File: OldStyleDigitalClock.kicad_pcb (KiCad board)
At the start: 2 copper layers, 155 x 85 mm, 89 parts, among them J1 USB_A_OUT, J2 USB_A_OUT, J3 USB_C_IN, SW1 Set minutes, SW2 Set hours, U1 4071, U10 CD4026BE, U11 NE555D, U12 CD4060BE, U13 CD4017BE, U14 CD4017BE, U15 CD4017BE, U2 D168K, U3 CD4026BE, U4 D168K, U5 CD4026BE, U6 4073, U7 D168K, U8 CD4026BE, U9 D168K, Y1 HC49 XTAL (32768 Hz)

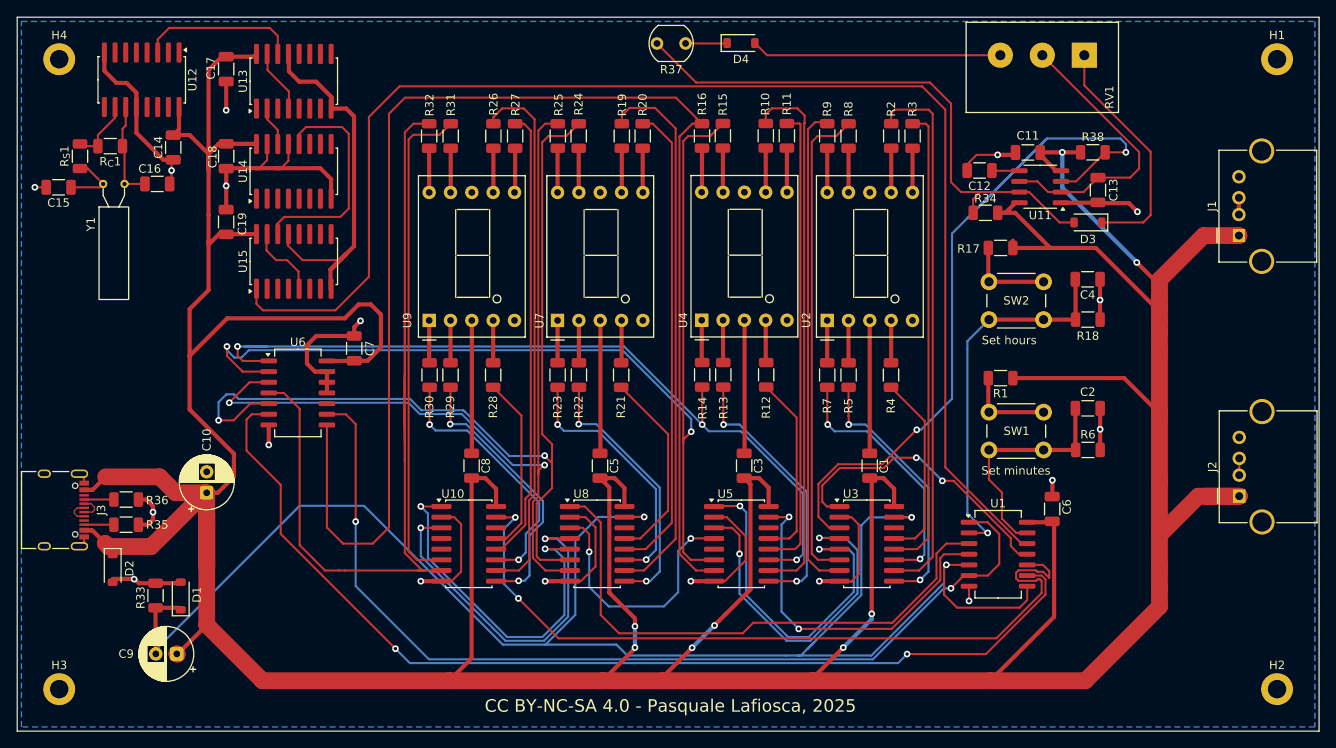
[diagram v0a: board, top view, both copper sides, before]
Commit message: Minor adjustments, moved oscillator away from mounting hole, improved some tracks.
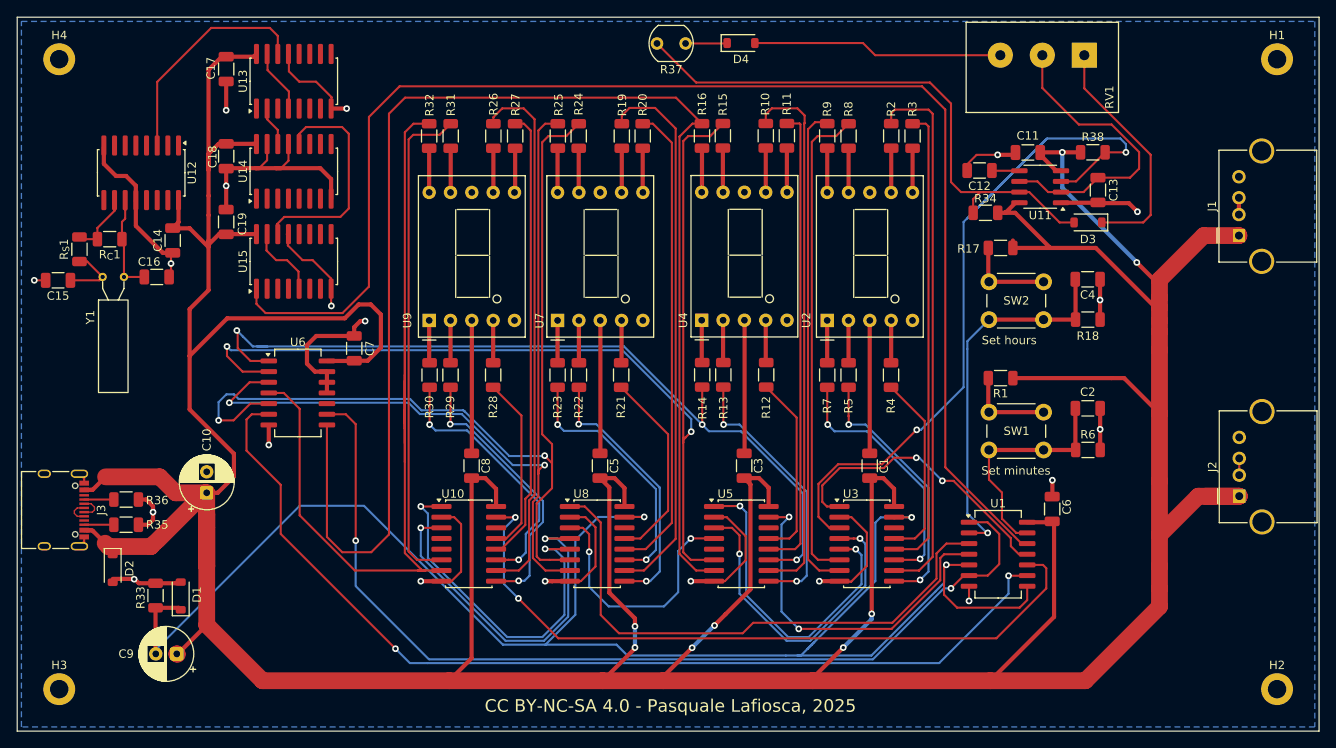
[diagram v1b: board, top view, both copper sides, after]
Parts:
- moved C15 11.1 mm to (54.9, 81.3)
- moved C16 11.1 mm to (66.6, 80.9)
- moved R_{C}1 11.1 mm to (61.0, 76.4)
- moved R_{S}1 11.1 mm to (57.4, 77.6)
- moved Y1 11.1 mm to (60.2, 80.9)
- moved C14 11.1 mm to (68.5, 76.6)
- moved U12 11.1 mm to (64.8, 68.5)
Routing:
- net GND: track 285.6 -> 263.5 mm, vias 18 -> 20
- net /Time/CLK 2 Hz: track 19.0 -> 27.1 mm
- net Net-(U10-RESET): track 93.3 -> 85.4 mm
- net /CLK 1/(24 hours): track 123.2 -> 119.0 mm
- net Net-(U3-CARRY_OUT): track 42.2 -> 38.8 mm
- net Net-(U3-DISPLAY_EN_OUT): track 41.7 -> 38.8 mm
- net Net-(U11-THR): track 34.2 -> 36.5 mm
- net Net-(U10-G): track 128.4 -> 126.3 mm
- net Net-(U5-G): track 167.7 -> 169.7 mm
- net Net-(U5-F): track 128.9 -> 127.9 mm
- net 1_MIN_CLK: track 163.6 -> 164.5 mm
- net MR: track 196.0 -> 195.2 mm

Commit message: Moved USB receptacles, minor changes. Marked no connect pins.
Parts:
- moved J1 3.71 mm to (191.8, 75.9)
- moved J2 3.71 mm to (191.8, 107.0)
- moved J3 0.40 mm to (53.9, 108.7)
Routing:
- net +5V: track 618.9 -> 607.5 mm
- net Net-(J3-D+-PadA6): track 2.93 -> 4.73 mm

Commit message: Reviewed LED limiting resistors to stay within specs
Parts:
- D2: value 1N4733A -> 1N4734A
- R10, R11, R12, R13, R14, R15, R16, R19, R2, R20, R21, R22, R23, R24, R25, R26, R27, R28, R29, R3, R30, R31, R32, R4, R5, R7, R8, R9: value 2.2 kΩ -> 4.7 kΩ

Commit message: Centering
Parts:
- moved C1 0.61 mm to (150.9, 103.4)
- moved C3 0.61 mm to (135.9, 103.4)
- moved R15 0.61 mm to (133.4, 64.1)
- moved R16 0.61 mm to (130.9, 64.1)
- moved R19 0.61 mm to (121.4, 64.1)
- moved R2 0.61 mm to (153.5, 64.1)
- moved R21 0.61 mm to (121.3, 92.6)
- moved R3 0.61 mm to (156.0, 64.1)
- moved R7 0.61 mm to (145.8, 92.6)
- moved R9 0.61 mm to (145.8, 64.1)
- moved U3 0.61 mm to (150.5, 112.7)
- moved C5 0.61 mm to (118.8, 103.4)
- moved C8 0.61 mm to (103.5, 103.4)
- moved R20 0.61 mm to (123.9, 64.1)
- moved R22 0.61 mm to (116.3, 92.6)
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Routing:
- net MR: track 195.2 -> 196.1 mm
- net Net-(U5-G): track 169.7 -> 169.1 mm
- net Net-(U5-E): track 99.2 -> 98.6 mm
- net LED_PWM: track 96.4 -> 97.0 mm
- net Net-(U5-RESET): track 42.5 -> 43.2 mm
- net Net-(U10-RESET): track 85.4 -> 86.0 mm
- net Net-(U8-G): track 106.4 -> 105.8 mm
- net Net-(U8-F): track 112.4 -> 111.8 mm
- net Net-(U8-CLK): track 66.6 -> 67.2 mm
- net Net-(U5-F): track 127.9 -> 127.3 mm
- net Net-(U3-CLK): track 35.3 -> 35.9 mm
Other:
- board text added: ":"

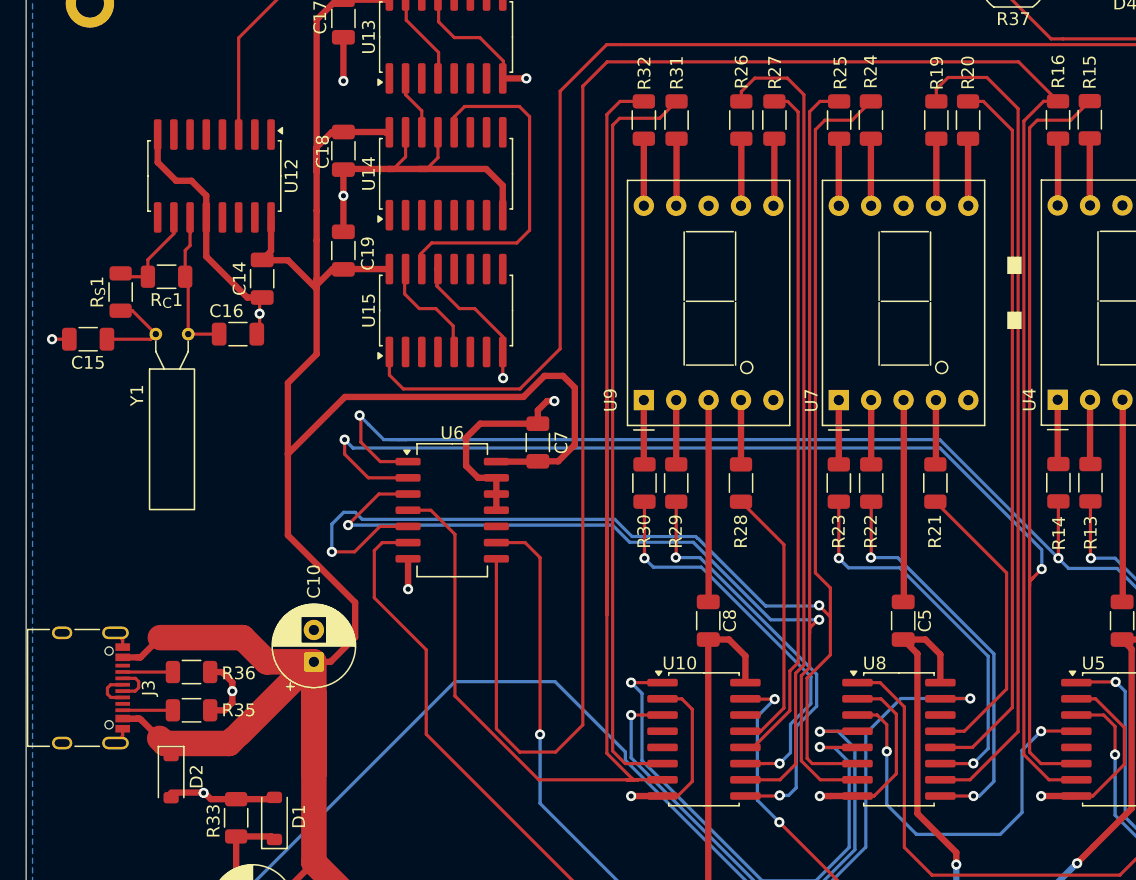
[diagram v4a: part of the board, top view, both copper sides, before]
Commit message: Redesigned USB C input in a more compact way.
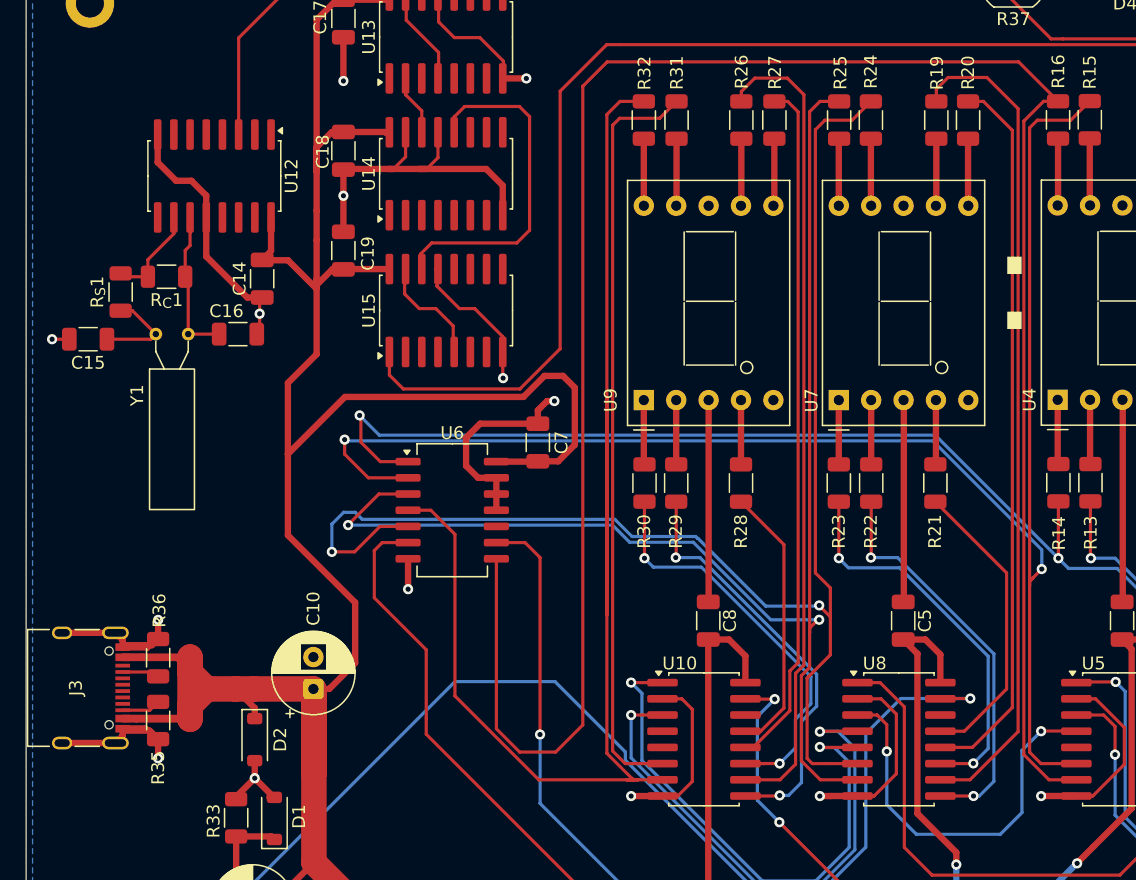
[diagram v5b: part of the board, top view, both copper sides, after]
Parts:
- moved D2 7.17 mm to (67.9, 112.7)
- moved R36 2.85 mm to (60.4, 106.3), turned to 90 degrees
- moved R35 2.74 mm to (60.4, 111.2), turned to -90 degrees
- moved C10 2.13 mm to (72.5, 108.8)
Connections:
- J3 pad A6: Net-(J3-D+-PadA6) -> unconnected-(J3-D+-PadA6)
- J3 pad A7: Net-(J3-D--PadA7) -> unconnected-(J3-D--PadA7)
- J3 pad B6: Net-(J3-D+-PadA6) -> unconnected-(J3-D+-PadB6)
- J3 pad B7: Net-(J3-D--PadA7) -> unconnected-(J3-D--PadB7)
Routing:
- net GND: track 263.5 -> 281.1 mm, vias 20 -> 21
- net +5V: track 607.2 -> 621.9 mm
- net Net-(J3-D+-PadA6): track 4.73 -> 0.00 mm
- net Net-(J3-D--PadA7): track 3.20 -> 0.00 mm
- net Net-(U5-E): track 98.6 -> 97.4 mm
- net Net-(J3-CC1): track 3.54 -> 2.45 mm
- net unconnected-(J3-D+-PadA6): track 0.00 -> 0.83 mm
- net unconnected-(J3-D+-PadB6): track 0.00 -> 0.82 mm

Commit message: Changed footprints for easy to find parts
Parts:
- U1, U6: footprint Package_SO:SO-14_5.3x10.2mm_P1.27mm -> Package_SO:SOIC-14_3.9x8.7mm_P1.27mm
- U10, U12, U13, U14, U15, U3, U5, U8: footprint Package_SO:SOIC-16W_5.3x10.2mm_P1.27mm -> Package_SO:SOP-16_3.9x9.9mm_P1.27mm

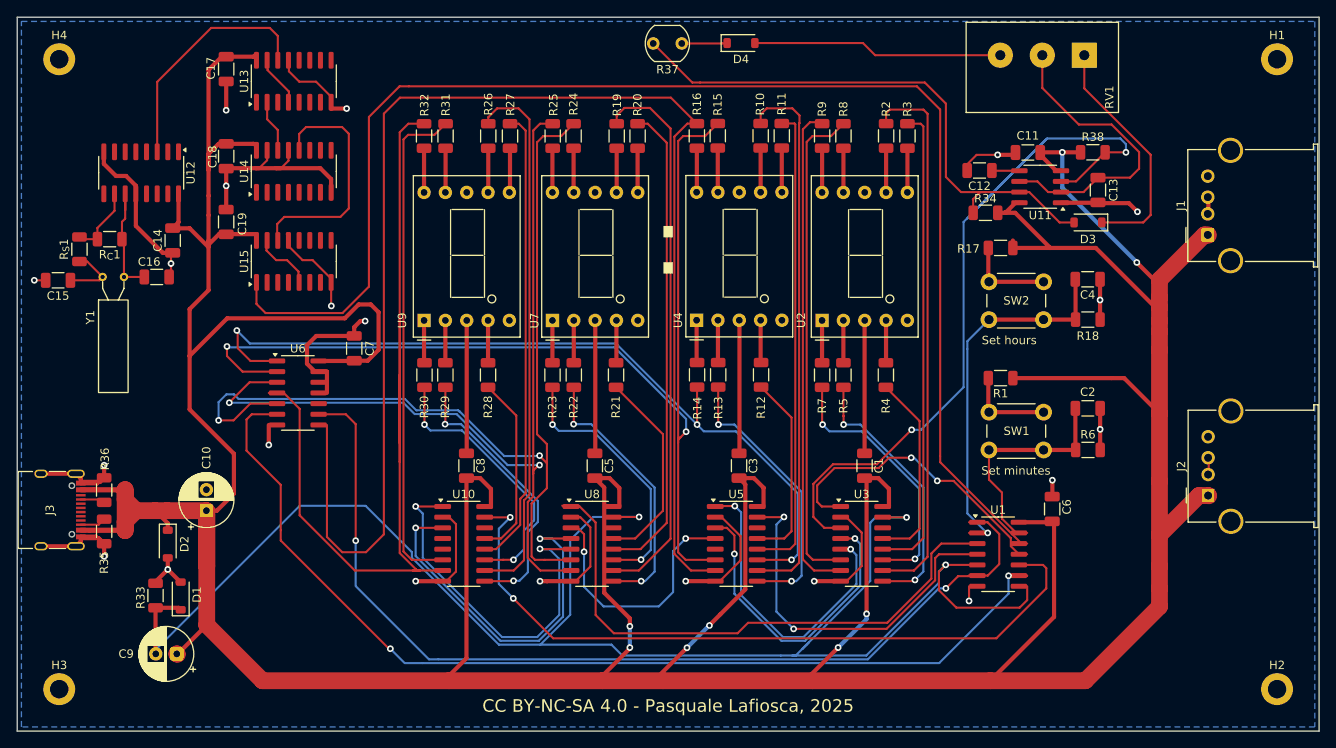
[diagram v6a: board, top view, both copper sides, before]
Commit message: Changed tracks for new IC packages
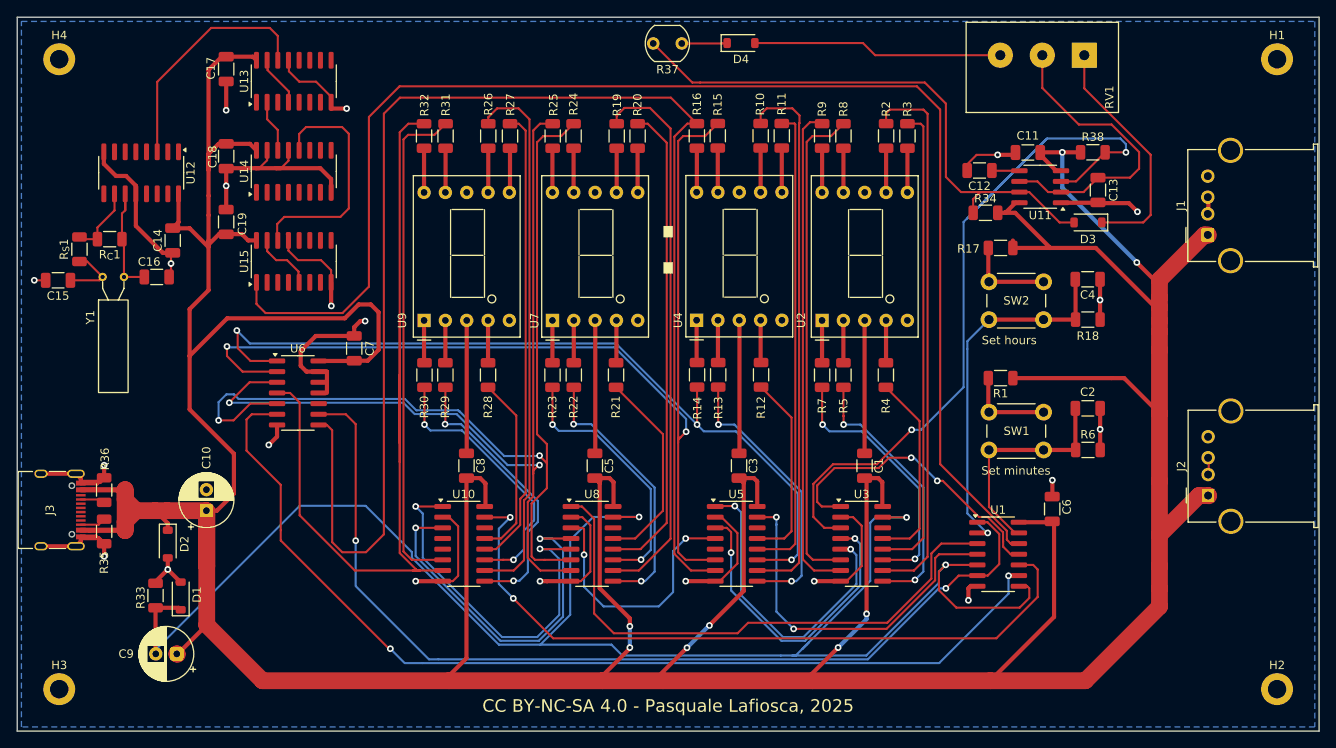
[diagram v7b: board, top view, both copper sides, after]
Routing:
- net GND: track 281.1 -> 288.2 mm
- net Net-(U10-RESET): track 86.0 -> 84.4 mm
- net +5V: track 621.9 -> 623.4 mm
- net Net-(U5-RESET): track 43.2 -> 41.9 mm
- net Net-(C2-Pad2): track 27.8 -> 26.6 mm
- net MR: track 196.1 -> 197.3 mm
- net Net-(U5-G): track 169.1 -> 170.1 mm
- net Net-(C4-Pad2): track 44.9 -> 43.9 mm
- net /CLK 1/hour: track 115.9 -> 114.9 mm
- net /CLK 1/(24 hours): track 119.5 -> 118.5 mm
- net Net-(U15-6): track 8.84 -> 8.06 mm
- net Net-(U3-CLK): track 35.9 -> 35.4 mm
- net Net-(U10-G): track 126.3 -> 125.8 mm

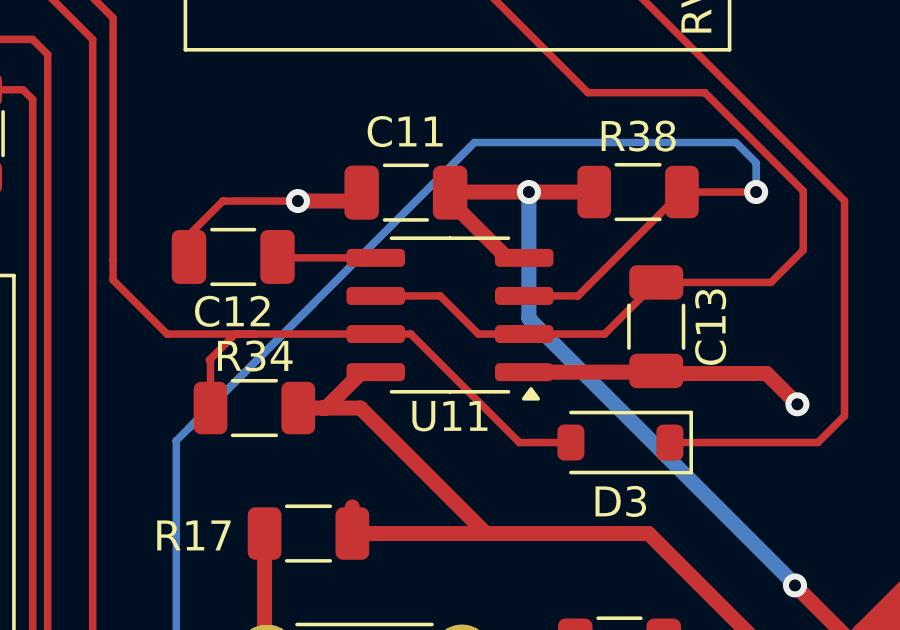
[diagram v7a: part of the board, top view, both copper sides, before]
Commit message: Updated NE555 package
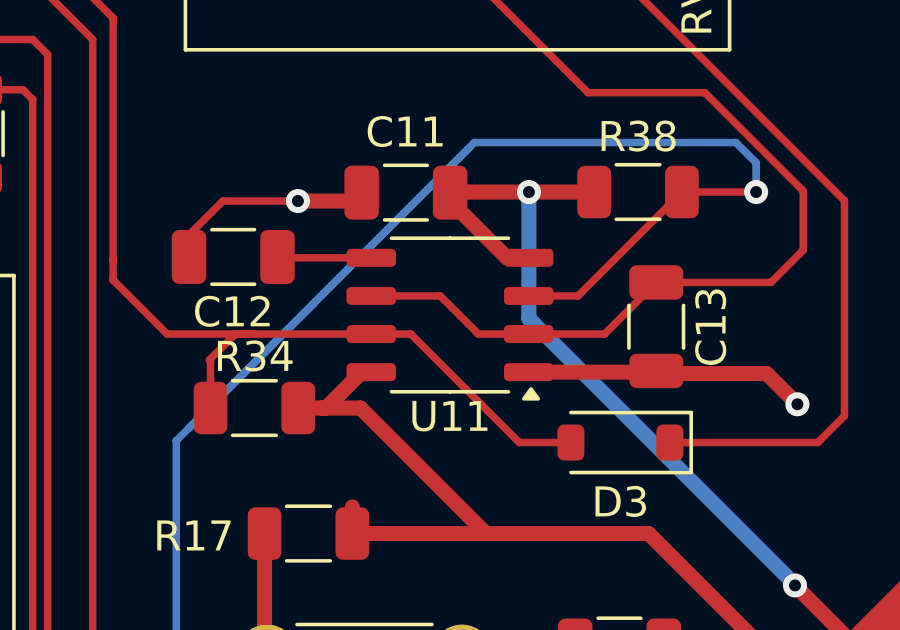
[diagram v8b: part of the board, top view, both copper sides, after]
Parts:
- U11: footprint Package_SO:SOIC-8_3.9x4.9mm_P1.27mm -> Package_SO:SOP-8_3.9x4.9mm_P1.27mm
